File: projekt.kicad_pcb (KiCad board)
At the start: 2 copper layers, 85 parts, among them IC1 DW01+G, J1 USB_C_Receptacle_PowerOnly_24P, J11 AO1, J12 BO2, J13 BO1, J14 BO1, J2 TP4056, J3 Conn_01x04_Pin, J4 Conn_01x02_Socket, J5 AO1, J6 USB_C_Receptacle_PowerOnly_6P, J7 AO2, J8 AO2, J9 BO2, Q1 AO3400A, Q2 AO3400A, Q3 AO3400A, Q4 AO3400A, Q5 AO3400A, Q6 AO3400A, SW1 SW_Slide_DPDT, SW2 RST, SW3 BOOT, U2 ESP32-WROOM-32E, U4 TB6612FNG, U7 AMS1117-3.3

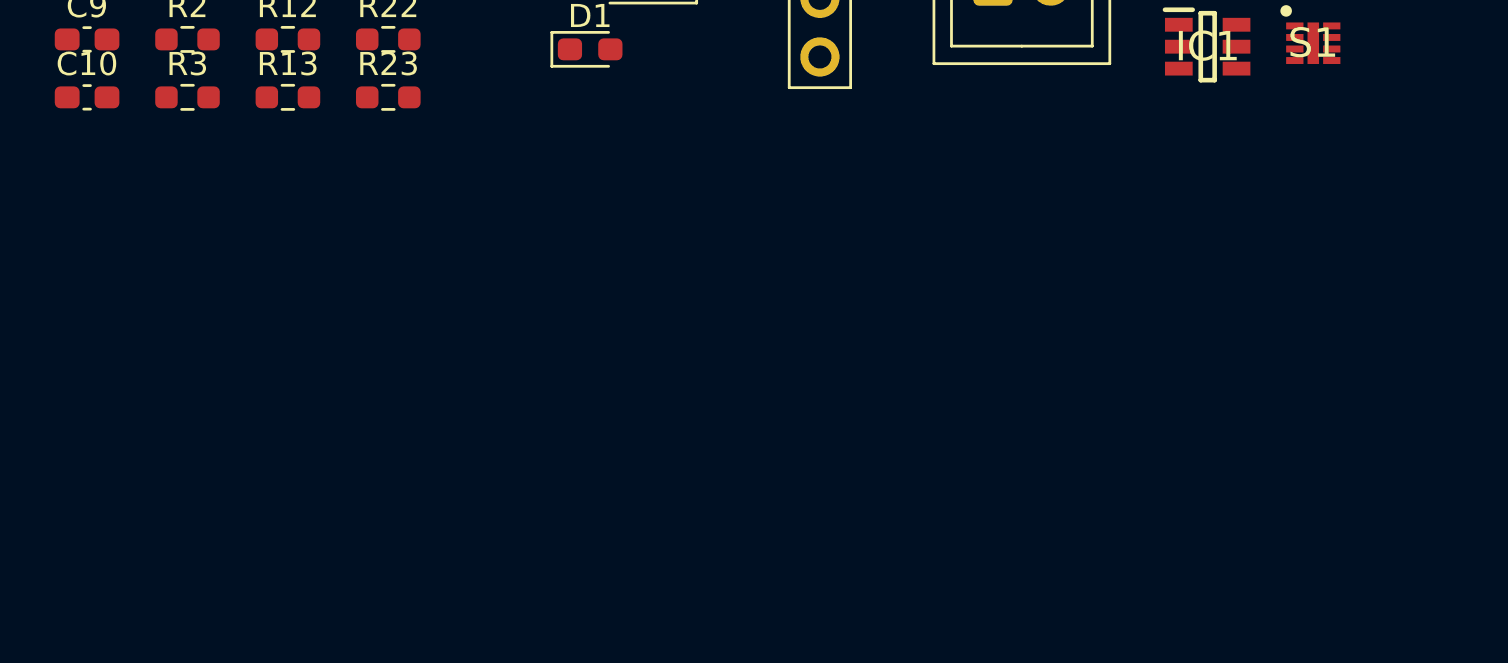
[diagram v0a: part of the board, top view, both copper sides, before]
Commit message: Dodanie drugiego DC IC
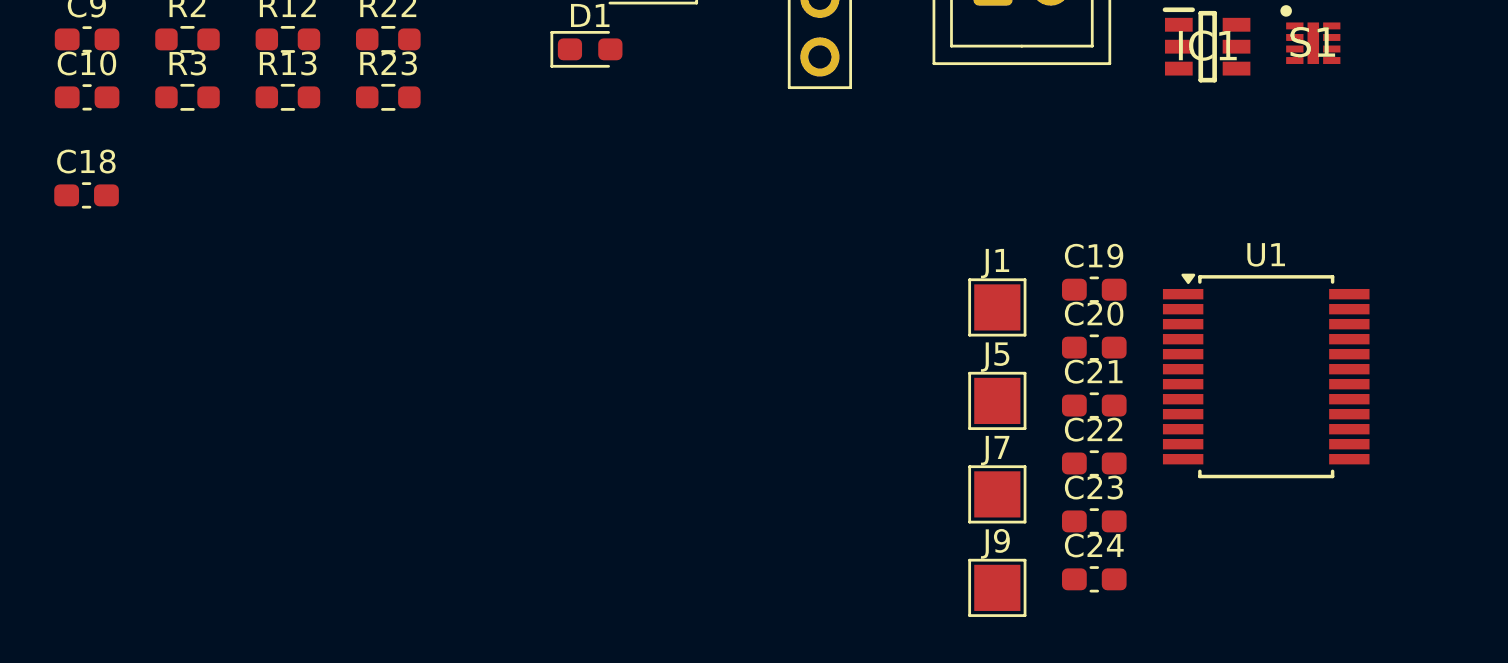
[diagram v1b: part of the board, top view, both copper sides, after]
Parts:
- added C18: 10u, Capacitor_SMD:C_0603_1608Metric_Pad1.08x0.95mm_HandSolder, F.Cu at (85.2, 116.6)
- added C19: 100n, Capacitor_SMD:C_0603_1608Metric_Pad1.08x0.95mm_HandSolder, F.Cu at (128.9, 120.7)
- added C20: 100n, Capacitor_SMD:C_0603_1608Metric_Pad1.08x0.95mm_HandSolder, F.Cu at (128.9, 123.2)
- added C21: 100n, Capacitor_SMD:C_0603_1608Metric_Pad1.08x0.95mm_HandSolder, F.Cu at (128.9, 125.7)
- added C22: 10u, Capacitor_SMD:C_0603_1608Metric_Pad1.08x0.95mm_HandSolder, F.Cu at (128.9, 128.2)
- added C23: 10u, Capacitor_SMD:C_0603_1608Metric_Pad1.08x0.95mm_HandSolder, F.Cu at (128.9, 130.7)
- added C24: 100n, Capacitor_SMD:C_0603_1608Metric_Pad1.08x0.95mm_HandSolder, F.Cu at (128.9, 133.2)
- added J1: CO1, TestPoint:TestPoint_Pad_2.0x2.0mm, F.Cu at (124.7, 121.4)
- added J5: CO2, TestPoint:TestPoint_Pad_2.0x2.0mm, F.Cu at (124.7, 125.5)
- added J7: DO1, TestPoint:TestPoint_Pad_2.0x2.0mm, F.Cu at (124.7, 129.5)
- added J9: DO2, TestPoint:TestPoint_Pad_2.0x2.0mm, F.Cu at (124.7, 133.6)
- added U1: TB6612FNG, Package_SO:SSOP-24_5.3x8.2mm_P0.65mm, F.Cu at (136.4, 124.4)
- C7: value 0.1u -> 100n
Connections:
- J14 pad 1: Net-(J13-Pin_1) -> Net-(J14-Pin_1)
- J8 pad 1: Net-(J7-Pin_1) -> Net-(J8-Pin_1)
- U2 pad 10: unconnected-(U2-IO25-Pad10) -> /IO25
- U2 pad 13: Net-(U2-IO14) -> /IO14
- U2 pad 14: Net-(U2-IO12) -> /IO12
- U2 pad 16: Net-(U2-IO13) -> /IO13
- U2 pad 23: Net-(U2-IO15) -> /IO15
- U2 pad 33: unconnected-(U2-IO21-Pad33) -> /IO21
- U4 pad 11: Net-(J13-Pin_1) -> Net-(J14-Pin_1)
- U4 pad 12: Net-(J13-Pin_1) -> Net-(J14-Pin_1)
- U4 pad 5: Net-(J7-Pin_1) -> Net-(J8-Pin_1)
- U4 pad 6: Net-(J7-Pin_1) -> Net-(J8-Pin_1)

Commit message: Praca nad PCB
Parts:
- removed the J1 at (124.7, 121.4)
- removed the J1 at (137.1, 93.4)
- removed J13: BO1, TestPoint:TestPoint_Pad_2.0x2.0mm
- removed J3: Conn_01x04_Pin, Connector_PinHeader_2.54mm:PinHeader_1x04_P2.54mm_Vertical
- removed the J5 at (124.7, 125.5)
- removed the J5 at (106.9, 90.5)
- removed the J7 at (106.9, 94.6)
- removed the J7 at (124.7, 129.5)
- removed the J9 at (124.7, 133.6)
- removed the J9 at (110.9, 90.5)
- removed TP2: TDI, TestPoint:TestPoint_Pad_2.0x2.0mm
- removed TP3: TCK, TestPoint:TestPoint_Pad_2.0x2.0mm
- removed TP4: TMS, TestPoint:TestPoint_Pad_2.0x2.0mm
- removed TP5: TDO, TestPoint:TestPoint_Pad_2.0x2.0mm
- added C25: 100n, Capacitor_SMD:C_0603_1608Metric_Pad1.08x0.95mm_HandSolder, F.Cu at (77.5, 97.4)
- added IC2: SS8050-HF, SamacSys_Parts:SOT95P240X115-3N, F.Cu at (177.1, 126.6)
- added IC3: SS8050-HF, SamacSys_Parts:SOT95P240X115-3N, F.Cu at (177.1, 132.9)
- added J1: CO1, TestPoint:TestPoint_Pad_2.0x2.0mm, F.Cu at (24.4, 189.7)
- added J10: Conn_01x06_Pin, Connector_PinHeader_2.54mm:PinHeader_1x06_P2.54mm_Vertical, F.Cu at (159.5, 123.2)
- added J5: CO2, TestPoint:TestPoint_Pad_2.0x2.0mm, F.Cu at (29.0, 190.0)
- added J7: DO1, TestPoint:TestPoint_Pad_2.0x2.0mm, F.Cu at (24.7, 183.4)
- added J9: DO2, TestPoint:TestPoint_Pad_2.0x2.0mm, F.Cu at (28.7, 183.4)
- added R28: 10k, Resistor_SMD:R_0603_1608Metric_Pad0.98x0.95mm_HandSolder, F.Cu at (172.8, 127.5)
- added R29: 10k, Resistor_SMD:R_0603_1608Metric_Pad0.98x0.95mm_HandSolder, F.Cu at (71.1, 102.3)
- added R30: 10k, Resistor_SMD:R_0603_1608Metric_Pad0.98x0.95mm_HandSolder, F.Cu at (54.0, 96.3)
- added R31: 10k, Resistor_SMD:R_0603_1608Metric_Pad0.98x0.95mm_HandSolder, F.Cu at (79.1, 91.2)
- J6: value USB_C_Receptacle_PowerOnly_6P -> USB_C_Receptacle_PowerOnly_24P; footprint Connector_USB:USB_C_Receptacle_GCT_USB4125-xx-x-0190_6P_TopMnt_Horizontal -> Connector_USB:USB_C_Receptacle_GCT_USB4110
- R8: value 100 -> 10k
- moved R1 168.4 mm to (254.9, 139.4)
- moved R2 163.2 mm to (250.1, 139.4), turned to 180 degrees
- moved C16 147.7 mm to (220.4, 33.7), turned to 180 degrees
- moved C15 146.6 mm to (223.3, 39.6), turned to 90 degrees
- moved C14 143.9 mm to (221.5, 39.6), turned to 90 degrees
- moved C4 139.3 mm to (221.7, 69.3), turned to 90 degrees
- moved R27 139.1 mm to (225.3, 31.7), turned to 90 degrees
- moved C1 137.1 mm to (221.7, 76.6), turned to 90 degrees
- moved R26 135.7 mm to (223.3, 32.5), turned to -90 degrees
- moved R25 134.3 mm to (226.0, 39.0), turned to 180 degrees
- moved R3 133.7 mm to (214.9, 65.6), turned to -90 degrees
- moved R4 128.3 mm to (220.0, 65.6), turned to -90 degrees
- moved R7 126.3 mm to (218.9, 78.9), turned to 90 degrees
- moved D6 125.4 mm to (123.2, 183.9)
- moved R5 122.9 mm to (216.2, 78.9), turned to 90 degrees
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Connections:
- net Net-(U2-EN) renamed /EN
- net Net-(U2-IO0) renamed /BOOT
- C5 pad 2: Net-(IC1-VCC) -> /LIPO+
- IC1 pad 5: Net-(IC1-VCC) -> /LIPO+
- R15 pad 1: GND -> Net-(IC2-B)
- R15 pad 2: /LED2 -> /DTR
- R8 pad 1: /LIPO+ -> GND
- R8 pad 2: Net-(IC1-VCC) -> Net-(R8-Pad2)
- SW3 pad 1: GND -> Net-(R8-Pad2)
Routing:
- net +3.3V: track 0.00 -> 2.45 mm
- net /EN: track 0.00 -> 2.43 mm
- net GND: track 0.00 -> 2.28 mm

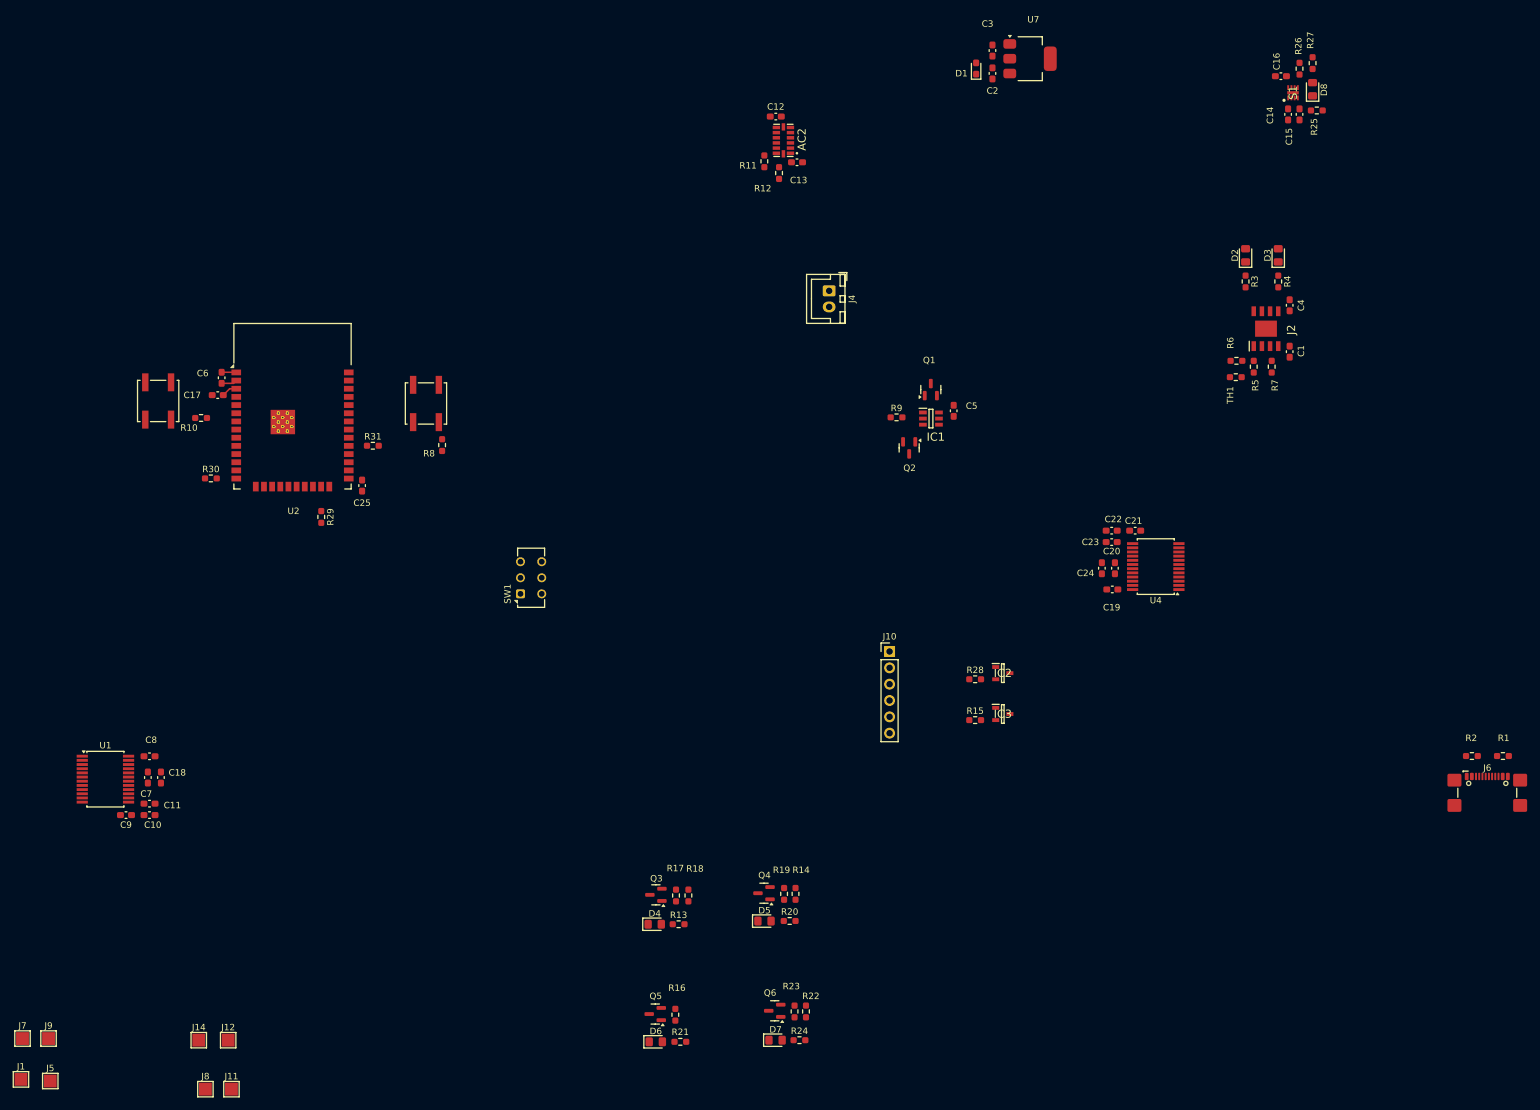
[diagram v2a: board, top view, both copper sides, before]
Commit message: wstępne ułożenie elementów
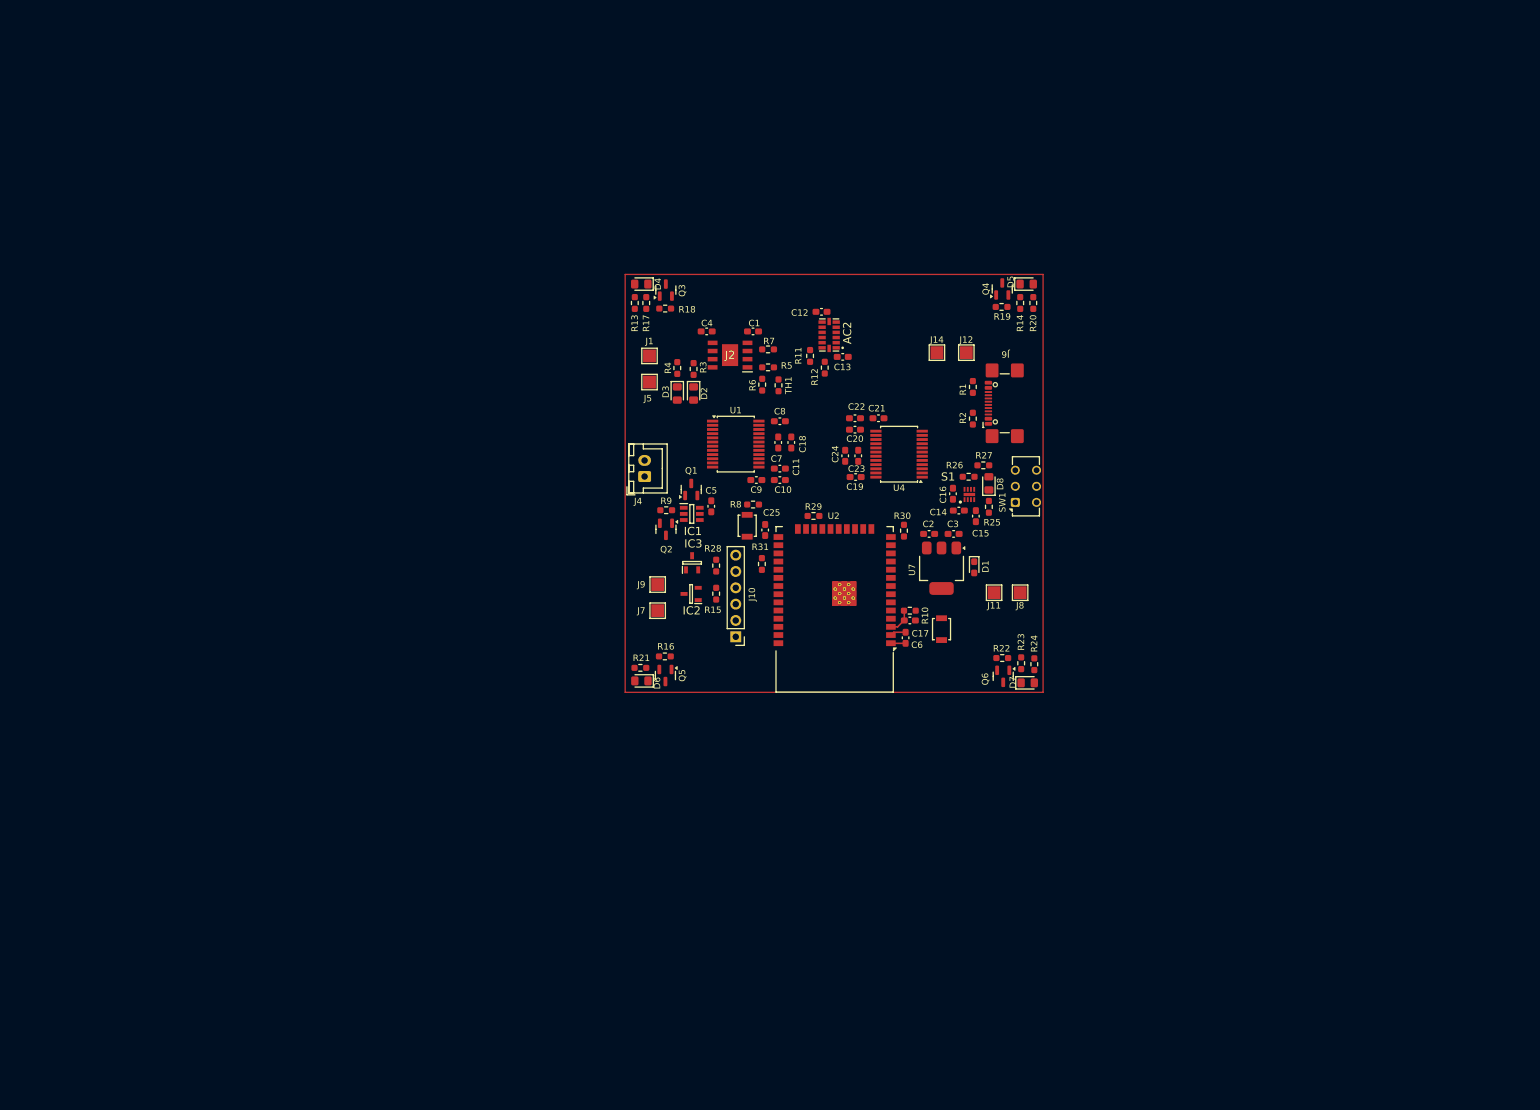
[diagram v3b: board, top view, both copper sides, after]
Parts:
- SW2, SW3: footprint Button_Switch_SMD:SW_Push_1P1T_NO_CK_KSC7xxJ -> Button_Switch_SMD:SW_SPST_B3U-1000P
- moved J12 156.9 mm to (171.4, 76.7)
- moved J14 156.9 mm to (166.9, 76.7)
- moved J1 149.1 mm to (122.2, 77.2), turned to 90 degrees
- moved J8 148.4 mm to (179.8, 114.0), turned to 180 degrees
- moved J5 143.2 mm to (122.2, 81.3), turned to 90 degrees
- moved J11 141.5 mm to (175.8, 114.0), turned to 180 degrees
- moved SW2 126.9 mm to (167.6, 119.7), turned to -90 degrees
- moved J7 119.1 mm to (123.4, 116.8), turned to -90 degrees
- moved J9 118.2 mm to (123.4, 112.8), turned to -90 degrees
- moved R10 114.2 mm to (162.7, 116.8), turned to 0 degrees
- moved C6 113.8 mm to (162.0, 121.1), turned to -90 degrees
- moved C17 113.2 mm to (162.7, 118.4), turned to 0 degrees
- moved C9 111.0 mm to (138.8, 96.5)
- moved C10 111.0 mm to (142.4, 96.5)
- moved C11 111.0 mm to (142.4, 94.7)
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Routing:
- net /EN: track 2.43 -> 4.03 mm

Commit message: Poprawienie schematu i PCB
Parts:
- removed D1: D, Diode_SMD:D_0603_1608Metric_Pad1.05x0.95mm_HandSolder
- removed IC2, IC3: SS8050-HF, SamacSys_Parts:SOT95P240X115-3N
- removed R22: 10k, Resistor_SMD:R_0603_1608Metric_Pad0.98x0.95mm_HandSolder
- removed U7: AMS1117-3.3, Package_TO_SOT_SMD:SOT-223-3_TabPin2
- added IC4: MIC5504-3.3YM5-TR, SamacSys_Parts:SOT95P280X145-5N, F.Cu at (163.3, 69.1)
- added Q7: SS8050-HF, SamacSys_Parts:SOT95P240X115-3N, F.Cu at (129.0, 109.8)
- added Q8: SS8050-HF, SamacSys_Parts:SOT95P240X115-3N, F.Cu at (128.9, 114.0)
- C3: value 4.7u -> 1u
- R13, R20: value 60 -> 120
- R21, R24: value 260 -> 320
- moved C2 36.2 mm to (160.3, 69.1), turned to -90 degrees
- moved C3 35.9 mm to (166.4, 69.1), turned to -90 degrees
- moved DO1 32.3 mm to (130.8, 85.3), turned to 180 degrees
- moved DO2 27.5 mm to (125.7, 85.3), turned to 180 degrees
- moved AO1 27.3 mm to (173.2, 86.9)
- moved AO2 27.3 mm to (177.3, 86.9)
- moved J6 24.4 mm to (179.1, 109.0)
- moved R1 24.4 mm to (173.0, 106.4)
- moved R2 24.4 mm to (173.0, 111.4)
- moved C1 20.2 mm to (147.8, 91.2), turned to 90 degrees
- moved R7 19.3 mm to (150.1, 93.0), turned to -90 degrees
- moved R5 19.1 mm to (149.4, 96.0)
- moved C4 18.4 mm to (141.2, 88.8), turned to 0 degrees
- moved J2 17.6 mm to (143.3, 92.5)
- moved R6 16.5 mm to (145.0, 97.3), turned to 180 degrees
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- renumbered J11 to AO1, J8 to AO2, J14 to BO1, J12 to BO2, J1 to CO1, J5 to CO2, J7 to DO1, J9 to DO2
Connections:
- net /IO13 renamed /PWMD
- net /IO14 renamed /DIN1
- net /IO19 renamed /PWMA
- net /IO21 renamed /CIN1
- net /IO22 renamed /AIN1
- net /IO23 renamed /AIN2
- net /IO25 renamed /CIN2
- net /IO26 renamed /BIN1
- net /IO27 renamed /BIN2
- C2 pad 1: /PWR+ -> /LIPO+
- R13 pad 2: +3V3 -> /PWR+
- R20 pad 2: +3V3 -> /PWR+
- R21 pad 2: +3V3 -> /PWR+
- R24 pad 2: +3V3 -> /PWR+
- U1 pad 16: /IO15 -> /DIN2
- U1 pad 19: /IO18 -> /BOOT
- U1 pad 23: /IO12 -> /PWMC
- U2 pad 14: /IO12 -> /PWMC
- U2 pad 23: /IO15 -> /LED3
- U2 pad 30: /IO18 -> /PWMB
- U2 pad 8: /LED3 -> /DIN2
- U4 pad 15: /IO18 -> /PWMB
- U4 pad 19: /IO18 -> /BOOT
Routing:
- net /EN: track 4.03 -> 2.48 mm

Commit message: powoli nabiera koloru
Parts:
- TH1: footprint Resistor_SMD:R_0603_1608Metric_Pad0.98x0.95mm_HandSolder -> Resistor_SMD:Termistor_SMD
- moved C2 24.7 mm to (153.2, 92.8)
- moved C3 24.7 mm to (159.3, 92.8)
- moved IC4 24.7 mm to (156.2, 92.8)
- moved C5 20.8 mm to (150.9, 92.3)
- moved IC1 20.8 mm to (147.8, 93.5)
- moved Q1 20.8 mm to (147.8, 89.1)
- moved Q2 20.8 mm to (143.3, 95.9)
- moved R9 20.8 mm to (143.3, 92.5)
- moved R4 16.2 mm to (121.7, 101.7)
- moved D3 16.2 mm to (121.7, 105.7)
- moved D2 16.2 mm to (124.2, 105.7)
- moved R3 16.2 mm to (124.2, 101.9)
- moved C1 12.2 mm to (135.6, 91.4)
- moved J2 12.2 mm to (131.1, 92.7)
- moved R5 12.2 mm to (137.2, 96.3)
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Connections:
- AC2 pad 1: +3V3 -> +3.3V
- AC2 pad 6: +3V3 -> +3.3V
- AC2 pad 7: +3V3 -> +3.3V
- C12 pad 1: +3V3 -> +3.3V
- C13 pad 1: +3V3 -> +3.3V
- C18 pad 1: +3V3 -> +3.3V
- C23 pad 1: +3V3 -> +3.3V
- C24 pad 1: +3V3 -> +3.3V
- C7 pad 1: +3V3 -> +3.3V
- R11 pad 1: +3V3 -> +3.3V
- R12 pad 2: +3V3 -> +3.3V
- R29 pad 1: /IO15 -> /LED3
- R30 pad 2: /IO12 -> /PWMC
- U1 pad 20: +3V3 -> +3.3V
- U4 pad 20: +3V3 -> +3.3V
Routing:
- net VCC: track 0.00 -> 94.6 mm
- net /LIPO+: track 0.00 -> 58.1 mm, vias 0 -> 1
- net /LED4: track 0.00 -> 55.5 mm, vias 0 -> 2
- net +3.3V: track 2.45 -> 56.2 mm, vias 0 -> 4
- net /LED3: track 0.00 -> 48.1 mm
- net /LED1: track 0.00 -> 44.9 mm, vias 0 -> 2
- net /SW+: track 0.00 -> 42.1 mm
- net /LIPO-: track 0.00 -> 36.7 mm
- net /PWR+: track 0.00 -> 32.5 mm, vias 0 -> 5
- net /LED2: track 0.00 -> 24.6 mm
- net /BOOT: track 0.00 -> 24.5 mm
- net Net-(J2-TEMP1): track 0.00 -> 14.1 mm
- net Net-(J2-~{STDBY}): track 0.00 -> 12.4 mm
- net Net-(AO2-Pin_1): track 0.00 -> 12.3 mm
- net Net-(BO2-Pin_1): track 0.00 -> 11.9 mm
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- added copper zone on In2.Cu, net +3.3V
- added copper zone on F.Cu, net /PWR+
- added copper zone on In1.Cu, net /PWR+
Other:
- board outline added: 65 x 65 mm
- copper layers 2 -> 4
